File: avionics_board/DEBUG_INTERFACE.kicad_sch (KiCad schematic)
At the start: 12 parts, among them J7 Conn_01x06, J8 Conn_01x04

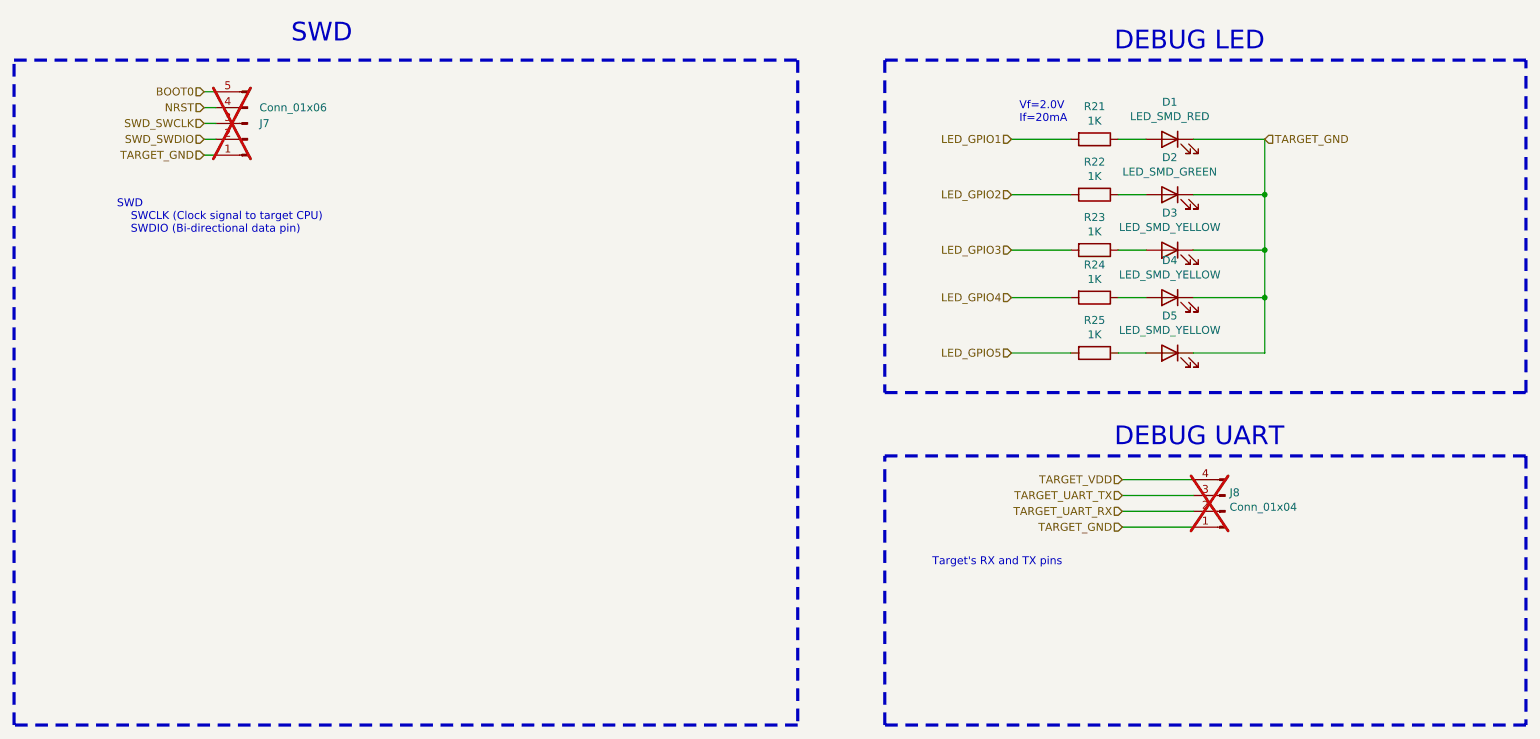
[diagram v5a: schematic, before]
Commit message: clenup BOM for SCI and AUX
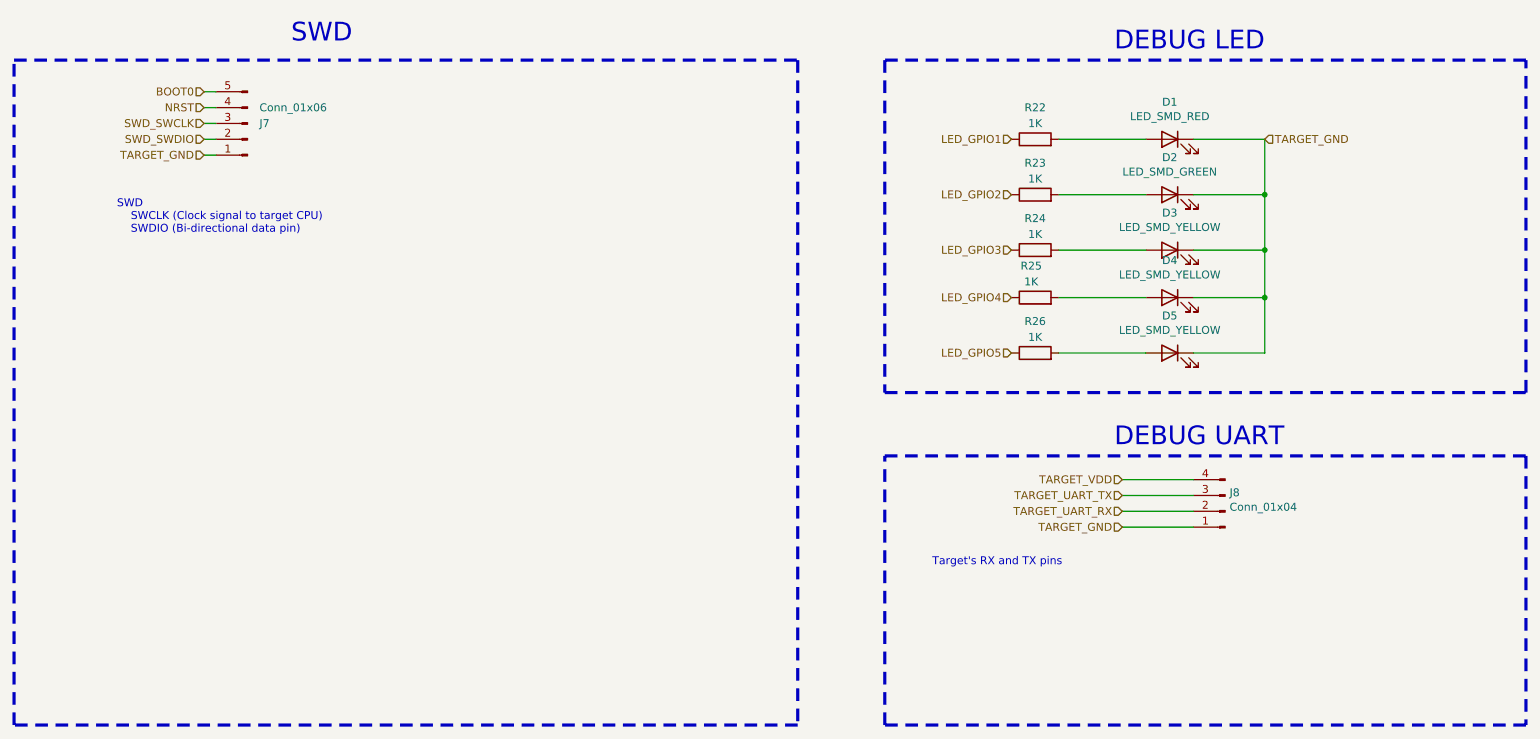
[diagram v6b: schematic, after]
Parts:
- removed R21: 1K, Resistor_SMD:R_0402_1005Metric_Pad0.72x0.64mm_HandSolder, symbol Device:R
- added R26: 1K, Resistor_SMD:R_0402_1005Metric_Pad0.72x0.64mm_HandSolder, symbol Device:R
- J7, J8: Manufacturer (none) -> generic; Part Number (none) -> generic; now fitted
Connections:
- net LED_GPIO1: now also R22.1
- net LED_GPIO2: now also R23.1; no longer R22.2
- net LED_GPIO3: now also R24.1; no longer R23.2
- net LED_GPIO4: now also R25.1; no longer R24.2
- net LED_GPIO5: now also R26.1; no longer R25.2
- net at D1.2 (A): now also R22.2
- net at D4.2 (A): now also R25.2; no longer R24.1
- net at D2.2 (A): now also R23.2; no longer R22.1
- net at D3.2 (A): now also R24.2; no longer R23.1
- net at D5.2 (A): now also R26.2; no longer R25.1
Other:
- note removed: "Vf=2.0V If=20mA"

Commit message: cleaning up bom: remove main camera port since it has not pullups and capacitors, correcting some errors in camera switch
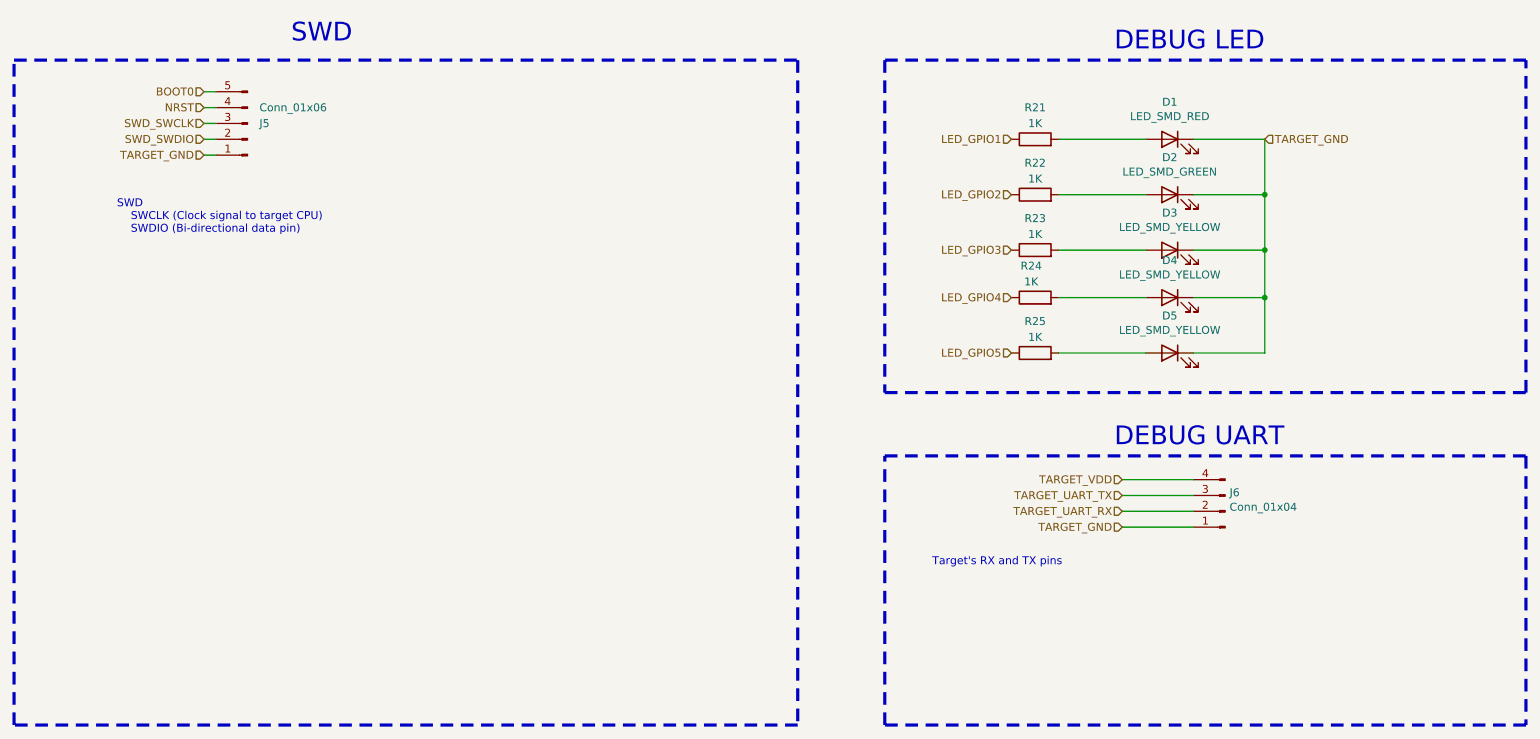
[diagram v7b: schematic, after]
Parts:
- renumbered J7 to J5, J8 to J6, R22 to R21, R23 to R22, R24 to R23, R25 to R24, R26 to R25
